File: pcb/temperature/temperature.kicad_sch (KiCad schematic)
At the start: 4 parts, among them J1 SM04B-GHS-TB, U1 TMP100

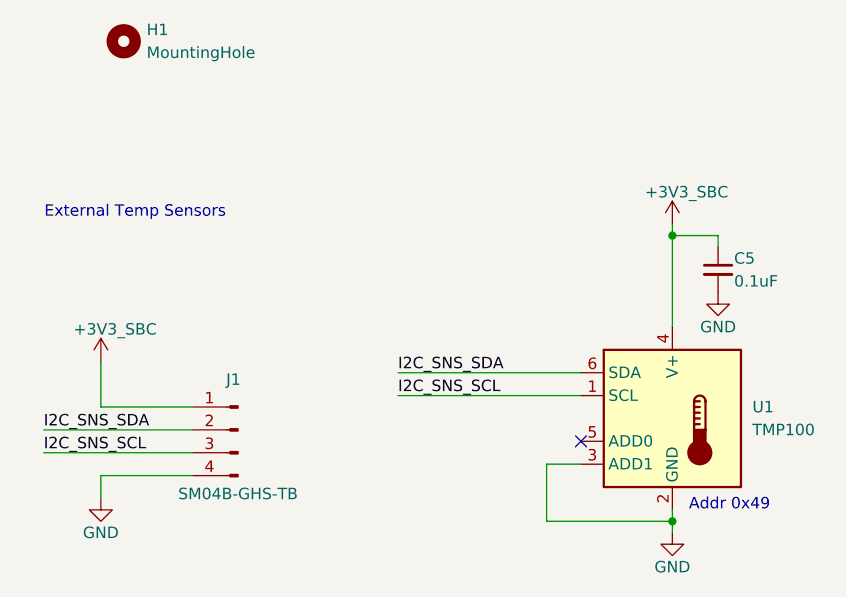
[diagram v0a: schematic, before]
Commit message: major overhaul for rflink. Python scripts for gr-dvbs rx/tx. Tested in loopback mode. Have not added mpeg pipeline yet. See readme for details. Exported pcb files for fab
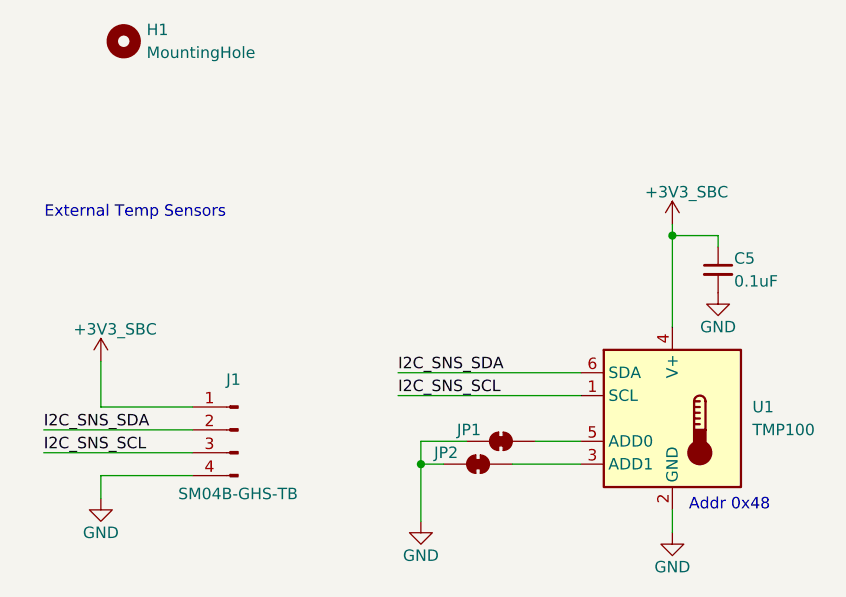
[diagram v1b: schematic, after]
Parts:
- added JP1, JP2: SolderJumper_2_Bridged, Jumper:SolderJumper-2_P1.3mm_Bridged_RoundedPad1.0x1.5mm, symbol Jumper:SolderJumper_2_Bridged
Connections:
- net GND: now also JP1.1 (A), JP2.1 (A); no longer U1.3 (ADD1)
- net at U1.5 (ADD0): now also JP1.2 (B)
- new net: JP2.2 (B), U1.3 (ADD1)
- no-connect marks 1 -> 0
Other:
- note added: "Addr 0x48"
- note removed: "Addr 0x49"
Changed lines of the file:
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@@
 	(generator_version "9.0")
 	(paper "A4")
-	(text "Addr 0x49"
+	(text "Addr 0x48"
 		(exclude_from_sim no)
 		(at 137.16 83.312 0)
@@
 	)
 	(junction
-		(at 130.81 85.09)
+		(at 102.87 78.74)
 		(diameter 0)
 		(color 0 0 0 0)
@@
 		(color 0 0 0 0)
 	)
-	(no_connect
-		(at 120.65 76.2)
-	)
 	(wire
 		(pts
@@
 	(wire
 		(pts
-			(xy 120.65 78.74) (xy 116.84 78.74)
+			(xy 107.95 76.2) (xy 102.87 76.2)
 		)
 		(stroke
@@
 	(wire
 		(pts
-			(xy 130.81 86.36) (xy 130.81 85.09)
+			(xy 130.81 83.82) (xy 130.81 86.36)
 		)
 		(stroke
@@
 	(wire
 		(pts
-			(xy 130.81 85.09) (xy 130.81 83.82)
+			(xy 115.57 76.2) (xy 120.65 76.2)
 		)
 		(stroke
@@
 	(wire
 		(pts
-			(xy 116.84 78.74) (xy 116.84 85.09)
+			(xy 102.87 78.74) (xy 105.41 78.74)
 		)
 		(stroke
@@
 	(wire
 		(pts
-			(xy 116.84 85.09) (xy 130.81 85.09)
+			(xy 113.03 78.74) (xy 120.65 78.74)
 		)
 		(stroke
@@
 	(wire
 		(pts
-			(xy 130.81 53.34) (xy 130.81 63.5)
+			(xy 102.87 78.74) (xy 102.87 85.09)
 		)
 		(stroke
@@
 	(wire
 		(pts
-			(xy 135.89 54.61) (xy 135.89 53.34)
+			(xy 102.87 76.2) (xy 102.87 78.74)
 		)
 		(stroke
@@
 		)
 	)
+	(wire
+		(pts
+			(xy 130.81 53.34) (xy 130.81 63.5)
+		)
+		(stroke
+			(width 0)
+			(type default)
+		)
+	)
+	(wire
+		(pts
+			(xy 135.89 54.61) (xy 135.89 53.34)
+		)
+		(stroke
+			(width 0)
+			(type default)
+		)
+	)
 	(image
-		(at 115.57 105.41)
+		(at 115.57 121.92)
 		(scale 0.306449)
 		(data "iVBORw0KGgoAAAANSUhEUgAAB8oAAAHiCAYAAACA1kbEAAAMTmlDQ1BJQ0MgUHJvZmlsZQAASImV"
@@
 	)
 	(symbol
+		(lib_id "Jumper:SolderJumper_2_Bridged")
+		(at 109.22 78.74 0)
+		(unit 1)
+		(exclude_from_sim no)
+		(in_bom no)
+		(on_board yes)
+		(dnp no)
+		(property "Reference" "JP2"
+			(at 105.664 77.47 0)
+			(effects
+				(font
+					(size 1.27 1.27)
+				)
+			)
+		)
+		(property "Value" "SolderJumper_2_Bridged"
+			(at 109.22 74.93 0)
+			(effects
+				(font
+					(size 1.27 1.27)
+				)
+				(hide yes)
+			)
+		)
+		(property "Footprint" "Jumper:SolderJumper-2_P1.3mm_Bridged_RoundedPad1.0x1.5mm"
+			(at 109.22 78.74 0)
+			(effects
+				(font
+					(size 1.27 1.27)
+				)
+				(hide yes)
+			)
+		)
+		(property "Datasheet" "~"
+			(at 109.22 78.74 0)
+			(effects
+				(font
+					(size 1.27 1.27)
+				)
+				(hide yes)
+			)
+		)
+		(property "Description" "Solder Jumper, 2-pole, closed/bridged"
+			(at 109.22 78.74 0)
+			(effects
+				(font
+					(size 1.27 1.27)
+				)
+				(hide yes)
+			)
+		)
+		(pin "2"
+		)
+		(pin "1"
+		)
+		(instances
+			(project "temperature"
+				(path "/3624b3a2-57d7-4f99-b89e-37f95765b967"
+					(reference "JP2")
+					(unit 1)
+				)
+			)
+		)
+	)
+	(symbol
 		(lib_id "power:GND")
 		(at 130.81 86.36 0)
@@
 					(unit 1)
 				)
+			)
+		)
+	)
+	(symbol
+		(lib_id "power:GND")
+		(at 102.87 85.09 0)
+		(unit 1)
+		(exclude_from_sim no)
+		(in_bom yes)
+		(on_board yes)
+		(dnp no)
+		(property "Reference" "#PWR01"
+			(at 102.87 91.44 0)
+			(effects
+				(font
+					(size 1.27 1.27)
+				)
+				(hide yes)
+			)
+		)
+		(property "Value" "GND"
+			(at 102.87 88.9 0)
+			(effects
+				(font
+					(size 1.27 1.27)
+				)
+			)
+		)
+		(property "Footprint" ""
+			(at 102.87 85.09 0)
+			(effects
+				(font
+					(size 1.27 1.27)
+				)
+				(hide yes)
+			)
+		)
+		(property "Datasheet" ""
+			(at 102.87 85.09 0)
+			(effects
+				(font
+					(size 1.27 1.27)
+				)
+				(hide yes)
+			)
+		)
+		(property "Description" "Power symbol creates a global label with name \"GND\" , ground"
+			(at 102.87 85.09 0)
+			(effects
+				(font
+					(size 1.27 1.27)
+				)
+				(hide yes)
+			)
+		)
+		(pin "1"
+		)
+		(instances
+			(project "temperature"
+				(path "/3624b3a2-57d7-4f99-b89e-37f95765b967"
+					(reference "#PWR01")
+					(unit 1)
+				)
+			)
+		)
+	)
+	(symbol
+		(lib_id "Jumper:SolderJumper_2_Bridged")
+		(at 111.76 76.2 0)
+		(unit 1)
+		(exclude_from_sim no)
+		(in_bom no)
+		(on_board yes)
+		(dnp no)
+		(property "Reference" "JP1"
+			(at 108.204 74.93 0)
+			(effects
+				(font
+					(size 1.27 1.27)
+				)
+			)
+		)
+		(property "Value" "SolderJumper_2_Bridged"
+			(at 111.76 72.39 0)
+			(effects
+				(font
+					(size 1.27 1.27)
+				)
+				(hide yes)
+			)
+		)
+		(property "Footprint" "Jumper:SolderJumper-2_P1.3mm_Bridged_RoundedPad1.0x1.5mm"
+			(at 111.76 76.2 0)
+			(effects
+				(font
+					(size 1.27 1.27)
+				)
+				(hide yes)
+			)
+		)
+		(property "Datasheet" "~"
+			(at 111.76 76.2 0)
+			(effects
+				(font
+					(size 1.27 1.27)
+				)
+				(hide yes)
+			)
+		)
+		(property "Description" "Solder Jumper, 2-pole, closed/bridged"
+			(at 111.76 76.2 0)
+			(effects
+				(font
+					(size 1.27 1.27)
+				)
+				(hide yes)
+			)
+		)
+		(pin "2"
+		)
+		(pin "1"
+		)
+		(instances
+			(project ""
+				(path "/3624b3a2-57d7-4f99-b89e-37f95765b967"
+					(reference "JP1")
+					(unit 1)
+				)
